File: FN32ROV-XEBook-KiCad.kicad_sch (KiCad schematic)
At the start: 60 parts, among them J2 USB-C 16P, Q1 UMH3NTN, Q2 DMP2035U-7, Q3 DMG2302U, U1 ESP32-WROVER-IE-N16R8, U2 CP2102N-A02-GQFN24R, U3 74LS07DR, U4 74LS07DR, U5 XC6220B331MR

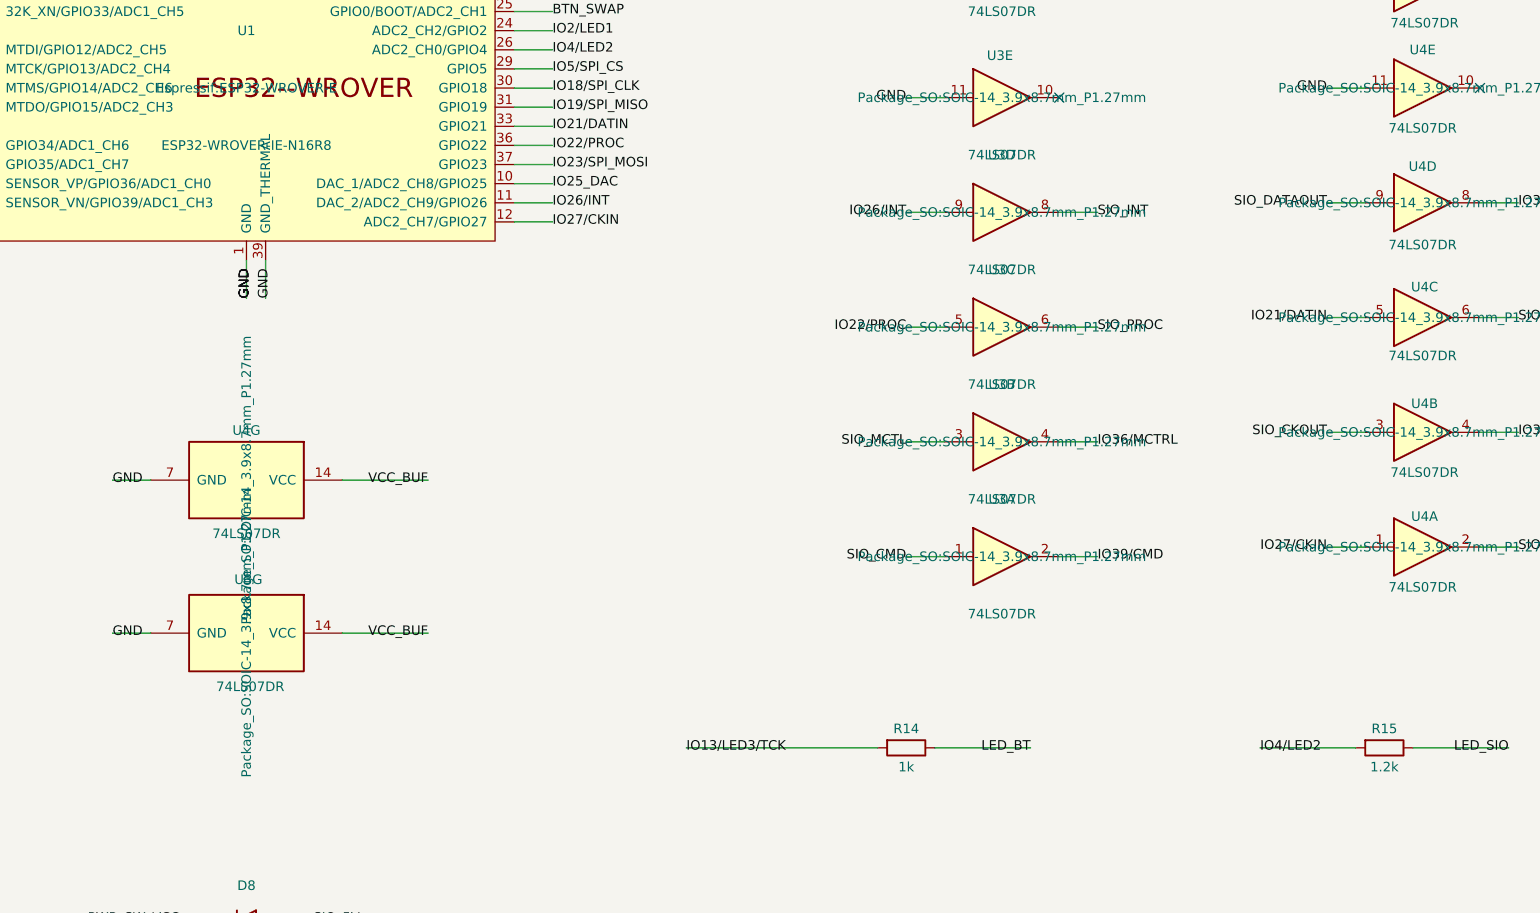
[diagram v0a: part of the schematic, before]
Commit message: Match LED brightness (R14 30k, R15 10K) and re-export fab for PCBWay
WiFi (R13 2.7k, green) was the channel the build is happy with; BT and SIO
read about twice as bright. Values come from a bench match on the LED board
at 3.33V with WiFi through its real 2.7k, not from calculation -- estimates
based on the 50%-dimming tape used as a stopgap landed near 2.4k and were
far off. The visual match was 9.2k on SIO; 10K was chosen deliberately as
slightly dimmer and already a basic part on this board.

  R13 WiFi green   2.7k  unchanged  C413089
  R14 BT   blue    1k -> 30k        C25776
  R15 SIO  orange  1.2k -> 10K      C25744

The 1.0 boards still carry 1k/1.2k and need hand-rework (0402s at y=67).

Fab re-export (Gerbers-FN32ROV-XEBook-1.1, never fabricated, so updated in
place): copper and drill came out identical to the 2026-08-01 export, which
also confirms the post-autoroute copper restore is exact. Only F.Silkscreen
changed, picking up the D4-D8 cathode bars and the corrected J_SIO1 vertical
header that were fixed in source after that export. Pick-and-place positions
and rotations are unchanged from what PCBWay assembled on 1.0.

Adds FN32ROV-XEBook-KiCad-BOM-PCBWay.xlsx/.csv as the file to send PCBWay:
same-part designators on one row (their explicit request), actual purchased
MPNs, the higher-voltage caps they substituted, J_SIO1 as BOOMELE 2.54-2*6P
(C9136), R13 on its own line. Verified against the schematic BOM and
pick-and-place: 60 placements, 28 lines. The plain BOM is now exported from
the schematic rather than hand-maintained.

Also folds in uncommitted work from earlier sessions: U1 -> ESP32-WROVER-E-
N16R8 (C529589) for the working PCB antenna, J_SIO1 -> Connector_IDC vertical
footprint, the unused Latch_Horizontal override's silk, removal of the two
superseded cable PDFs, and PCBWay's rev-1.0 question photos (D4/D5/D6 and
J_SIO1 orientation). .dsn is now gitignored as a regenerable export.

Co-Authored-By: Claude Opus 5 (1M context) <noreply@anthropi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
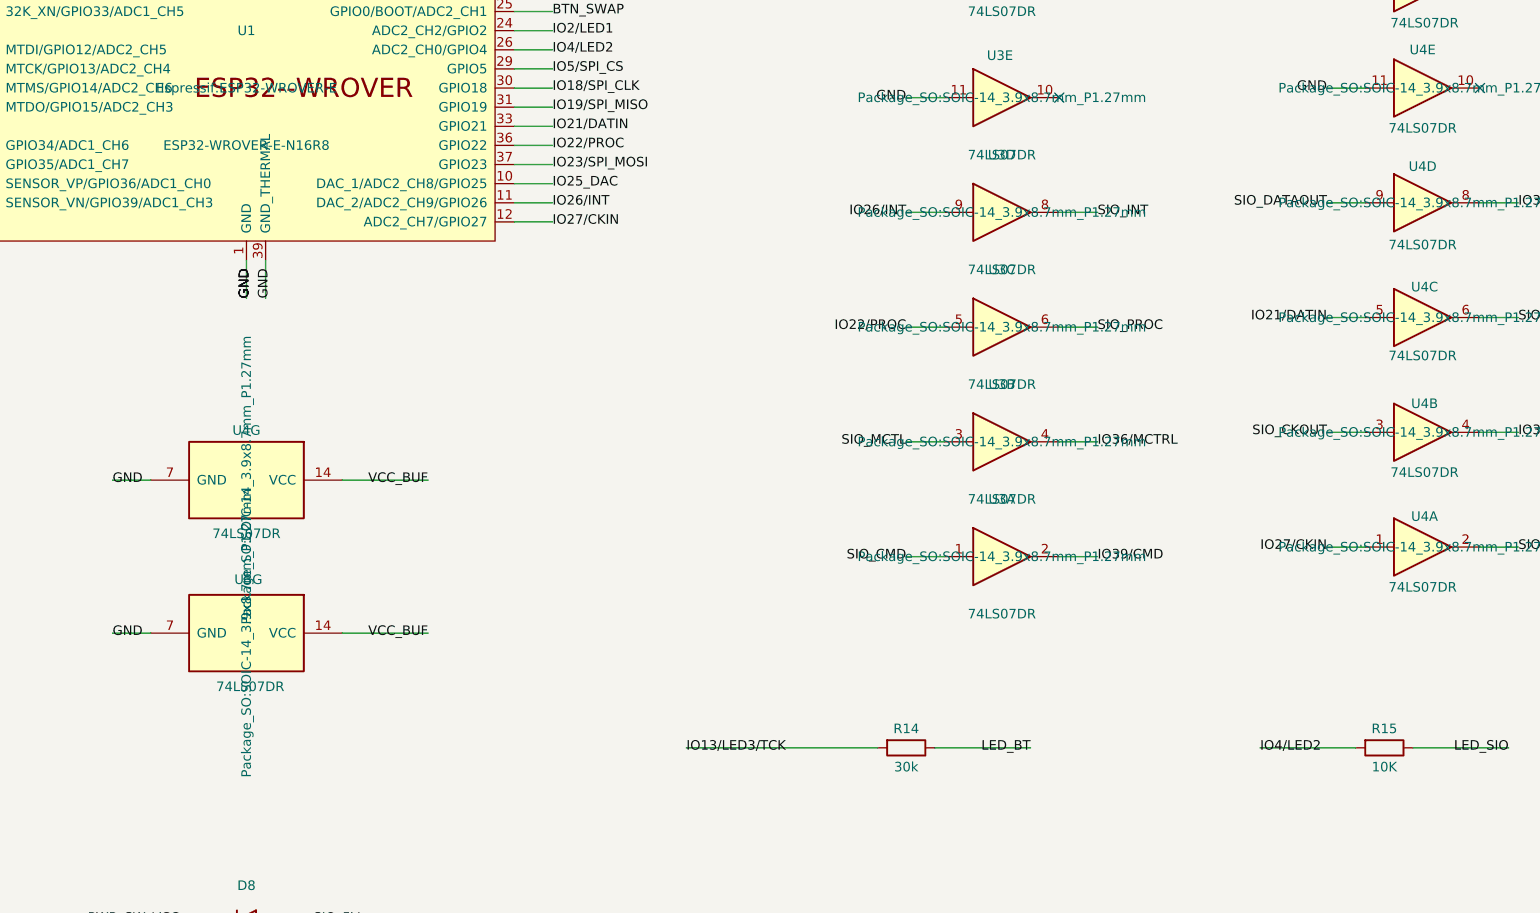
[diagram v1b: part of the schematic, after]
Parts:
- J_SIO1: footprint LocalOverrides:IDC-Header_2x06_P2.54mm_Latch_Horizontal -> Connector_IDC:IDC-Header_2x06_P2.54mm_Vertical
- R14: value 1k -> 30k
- R15: value 1.2k -> 10K
- U1: value ESP32-WROVER-IE-N16R8 -> ESP32-WROVER-E-N16R8
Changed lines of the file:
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@@
 			)
 		)
-		(property "Footprint" "LocalOverrides:IDC-Header_2x06_P2.54mm_Latch_Horizontal"
+		(property "Footprint" "Connector_IDC:IDC-Header_2x06_P2.54mm_Vertical"
 			(at 50.8 50.8 0)
 			(effects
@@
 			)
 		)
-		(property "Value" "1.2k"
+		(property "Value" "10K"
 			(at 304.8 281.94 90)
 			(effects
@@
 			)
 		)
-		(property "Value" "ESP32-WROVER-IE-N16R8"
+		(property "Value" "ESP32-WROVER-E-N16R8"
 			(at 153.67 199.39 0)
 			(effects
@@
 			)
 		)
-		(property "Value" "1k"
+		(property "Value" "30k"
 			(at 241.3 281.94 90)
 			(effects

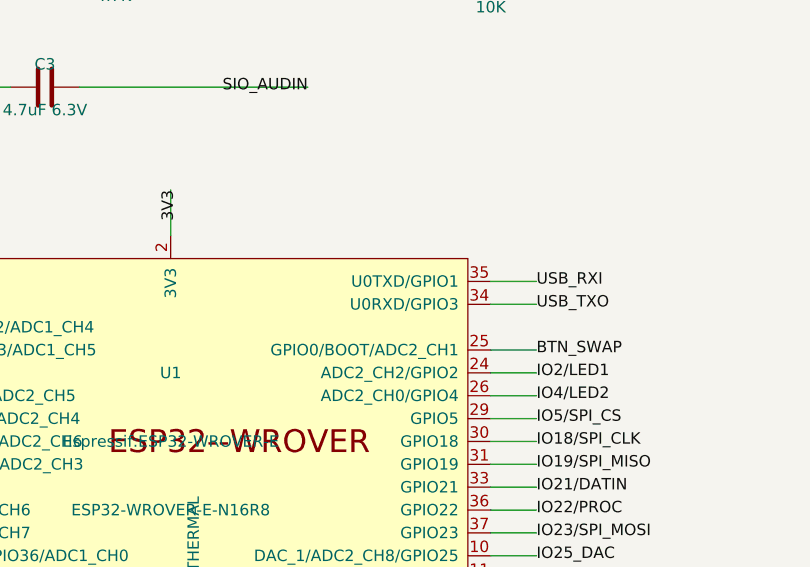
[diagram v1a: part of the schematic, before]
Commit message: Add TP1 SIO audio take-off pad for PokeyMax and re-export fab
A 2.0mm through-hole pad (1.0mm drill) on SIO_AUDIN at (80.475, 56.475),
routed back to J_SIO1 pad 10, so the PokeyMax J2 pin 4 wire has a proper
solder point instead of being tacked onto the back of the IDC header.

Sits in the open area right of J_SIO1, centred in a GND stitching-via cell
above the USB-C connector: 0.82mm to the four nearest vias, 1.1mm clear of
each via column along the route. Silkscreens SIO_AUDIN; the reference is
set not to print.

Marked exclude-from-BOM and exclude-from-position-files, so the BOM stays
at 30 rows and the pick-and-place at 60 placements -- both byte-identical
to the previous 1.1 export, and the hand-mapped PCBWay BOM needs no
revision.

Verification: netlist has TP1 pin 1 on /SIO_AUDIN alongside C3 pin 1 and
J_SIO1 pad 10; DRC reports 0 unconnected, 0 schematic-parity and no
violations involving TP1; no existing pad changed position or net
(280 -> 281 pads, the addition is TP1). Zones refilled, which also cleared
10 pre-existing stale-fill violations (4 hole-clearance, 4 starved-thermal,
2 footprint issues) -- total DRC went 22 -> 12, the remainder all
pre-existing and unrelated.

Fab re-exported into Gerbers-FN32ROV-XEBook-1.1 with the documented
settings (--subtract-soldermask, %LPC=1 confirmed). Against the previous
export only F.Cu, B.Cu, F/B mask, F/B silkscreen and the PTH drill differ;
Edge.Cuts, both paste layers, the NPTH drill and the job file are
unchanged. The PTH drill gains exactly one hole.

Co-Authored-By: Claude Opus 5 (1M context) <noreply@anthropic.com>
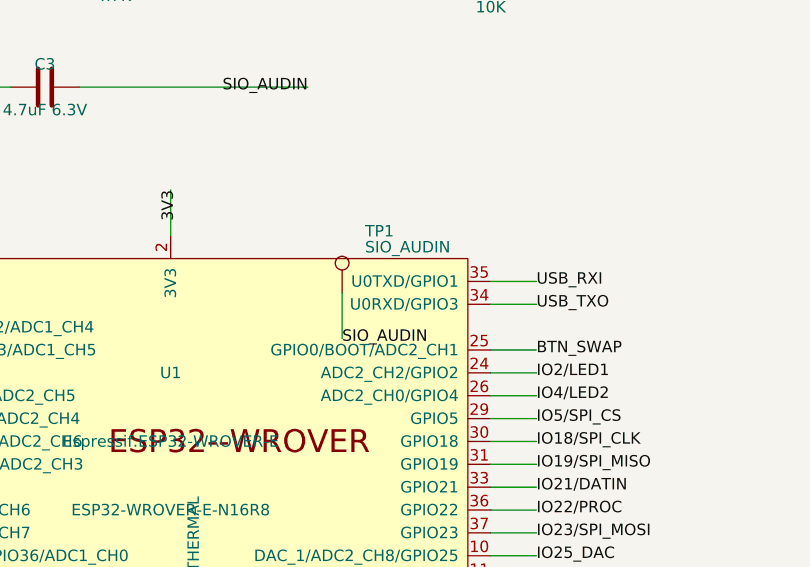
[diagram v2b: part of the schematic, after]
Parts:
- added TP1: SIO_AUDIN, TestPoint:TestPoint_THTPad_D2.0mm_Drill1.0mm, symbol Connector:TestPoint
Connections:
- net SIO_AUDIN: now also TP1.1
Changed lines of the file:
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@@
+		)
+	)
+	(symbol
+		(lib_id "Connector:TestPoint")
+		(at 172.72 175.26 0)
+		(unit 1)
+		(exclude_from_sim no)
+		(in_bom no)
+		(on_board yes)
+		(dnp no)
+		(property "Reference" "TP1"
+			(at 175.26 168.402 0)
+			(effects
+				(font
+					(size 1.27 1.27)
+				)
+				(justify left)
+			)
+		)
+		(property "Value" "SIO_AUDIN"
+			(at 175.26 170.17999999999998 0)
+			(effects
+				(font
+					(size 1.27 1.27)
+				)
+				(justify left)
+			)
+		)
+		(property "Footprint" "TestPoint:TestPoint_THTPad_D2.0mm_Drill1.0mm"
+			(at 172.72 175.26 0)
+			(effects
+				(font
+					(size 1.27 1.27)
+				)
+				(hide yes)
+			)
+		)
+		(property "Datasheet" "~"
+			(at 172.72 175.26 0)
+			(effects
+				(font
+					(size 1.27 1.27)
+				)
+				(hide yes)
+			)
+		)
+		(property "Description" "test point"
+			(at 172.72 175.26 0)
+			(effects
+				(font
+					(size 1.27 1.27)
+				)
+				(hide yes)
+			)
+		)
+		(pin "1"
+		)
+		(instances
+			(project "FN32ROV-XEBook-KiCad"
+				(path "/4c3930ed-aadd-48ff-beab-e5d9c5d47b74"
+					(reference "TP1")
+					(unit 1)
+				)
+			)
+		)
+	)
+	(wire
+		(pts
+			(xy 172.72 175.26) (xy 172.72 180.34)
+		)
+		(stroke
+			(width 0)
+			(type default)
+		)
+	)
+	(label "SIO_AUDIN"
+		(at 172.72 180.34 0)
+		(effects
+			(font
+				(size 1.27 1.27)
+			)
+			(justify left)
 		)
 	)
